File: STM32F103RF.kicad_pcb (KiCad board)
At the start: 4 copper layers, 64.8 x 24.1 mm, 56 parts, among them J1 USB_C_Receptacle_USB2.0, J2 Conn_01x04, J3 Conn_Coaxial, U1 SPX3819M5-L-3-3, U2 STM32F103C6Tx, U3 NRF24L01, Y1 16MHz, Y2 16MHz

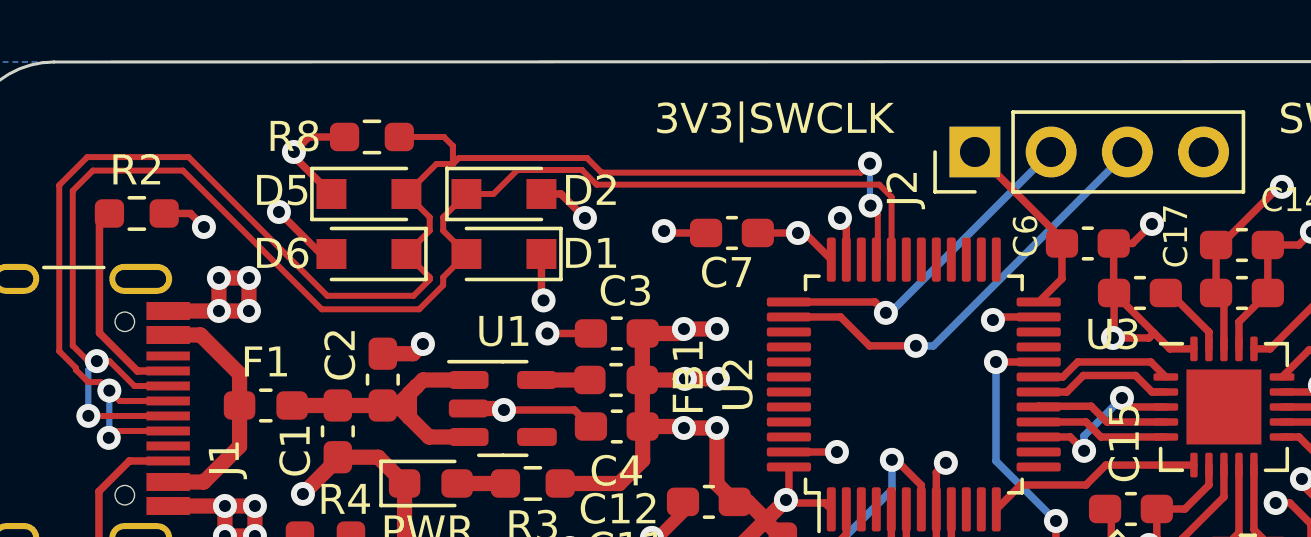
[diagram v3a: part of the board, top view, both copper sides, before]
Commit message: added proper ESD Protection for USB
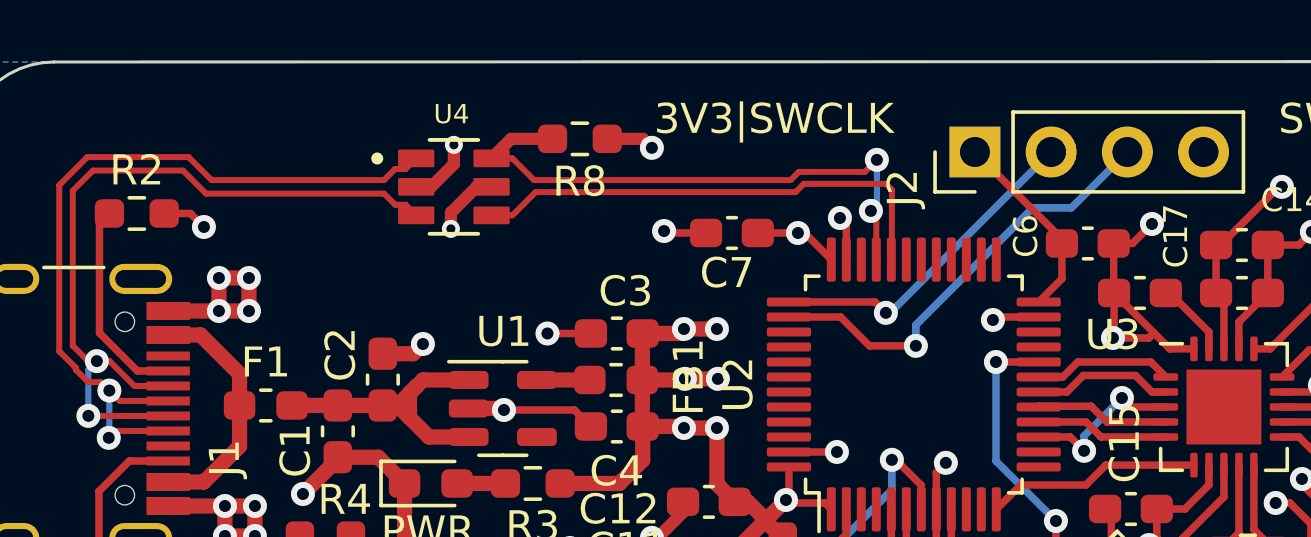
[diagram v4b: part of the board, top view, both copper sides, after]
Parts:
- removed D1, D2, D5, D6: D_Zener_Small, Diode_SMD:D_SOD-323_HandSoldering
- added U4: USBLC6-2SC6, SnapEDA Library:SOT95P280X145-6N, F.Cu at (83.6, 55.4)
- moved R8 6.93 mm to (87.8, 53.8), turned to 180 degrees
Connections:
- J1 pad A6: USB_D+ -> USBCON_D+
- J1 pad A7: USB_D- -> USBCON_D-
- J1 pad B6: USB_D+ -> USBCON_D+
- J1 pad B7: USB_D- -> USBCON_D-
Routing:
- net USB_D+: track 54.4 -> 19.3 mm, vias 4 -> 2
- net USB_D-: track 49.4 -> 16.4 mm, vias 2 -> 0
- net USBCON_D+: track 0.00 -> 26.5 mm, vias 0 -> 2
- net USBCON_D-: track 0.00 -> 25.9 mm, vias 0 -> 2
- net GND: track 232.4 -> 230.5 mm, vias 63 -> 62
- net 3.3V: track 63.2 -> 61.7 mm
